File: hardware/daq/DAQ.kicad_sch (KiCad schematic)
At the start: 185 parts, among them J1 ICD15S13E4GX00LF, J2 ICD15S13E4GX00LF, J4 ICD15S13E4GX00LF, J5 ICD15S13E4GX00LF, P1 0022272021, U1 ADS124S08IRHBT, U11 SN74AHCT125RGYR, U2 ADS124S08IRHBT, U3 LT6654BMPS6-5-TRMPBF, U4 LM1086IS-5.0_NOPB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

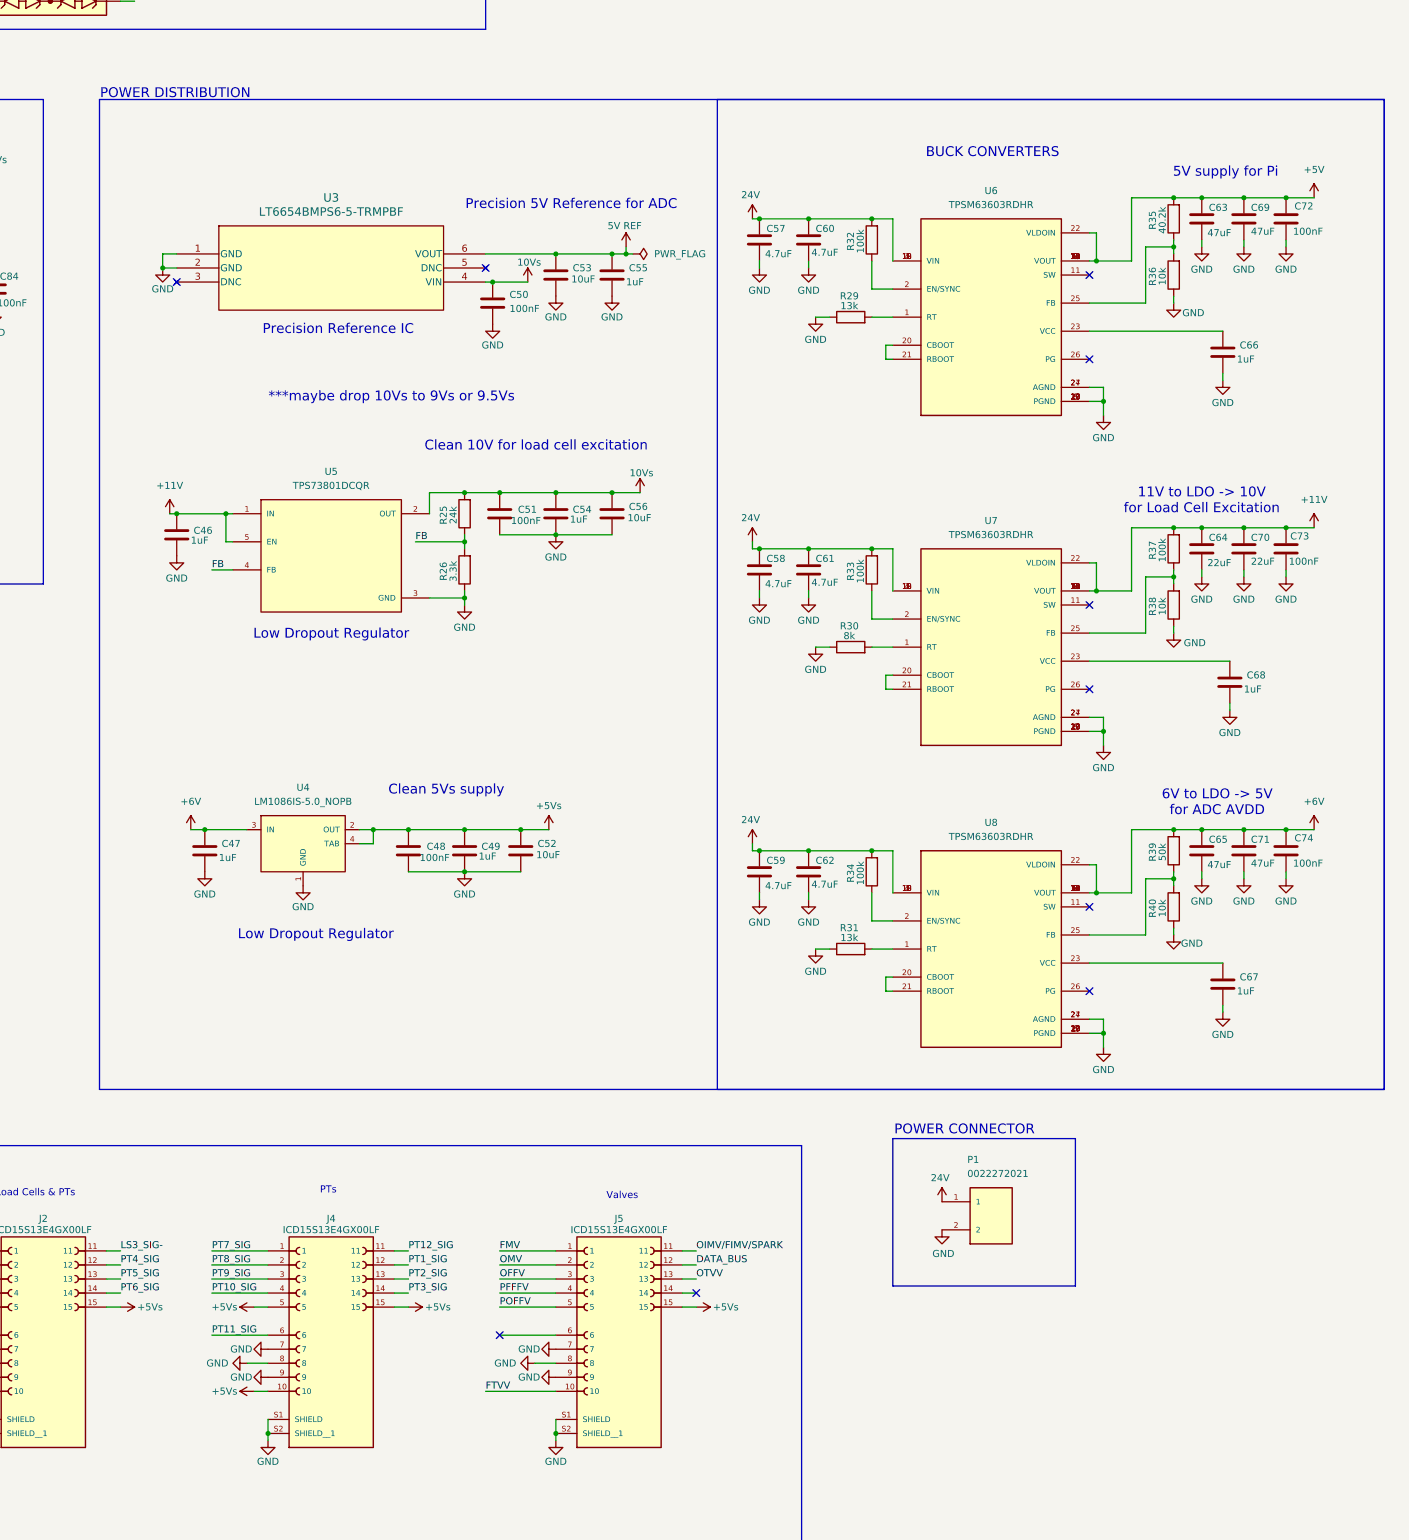
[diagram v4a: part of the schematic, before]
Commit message: more ERC fixes
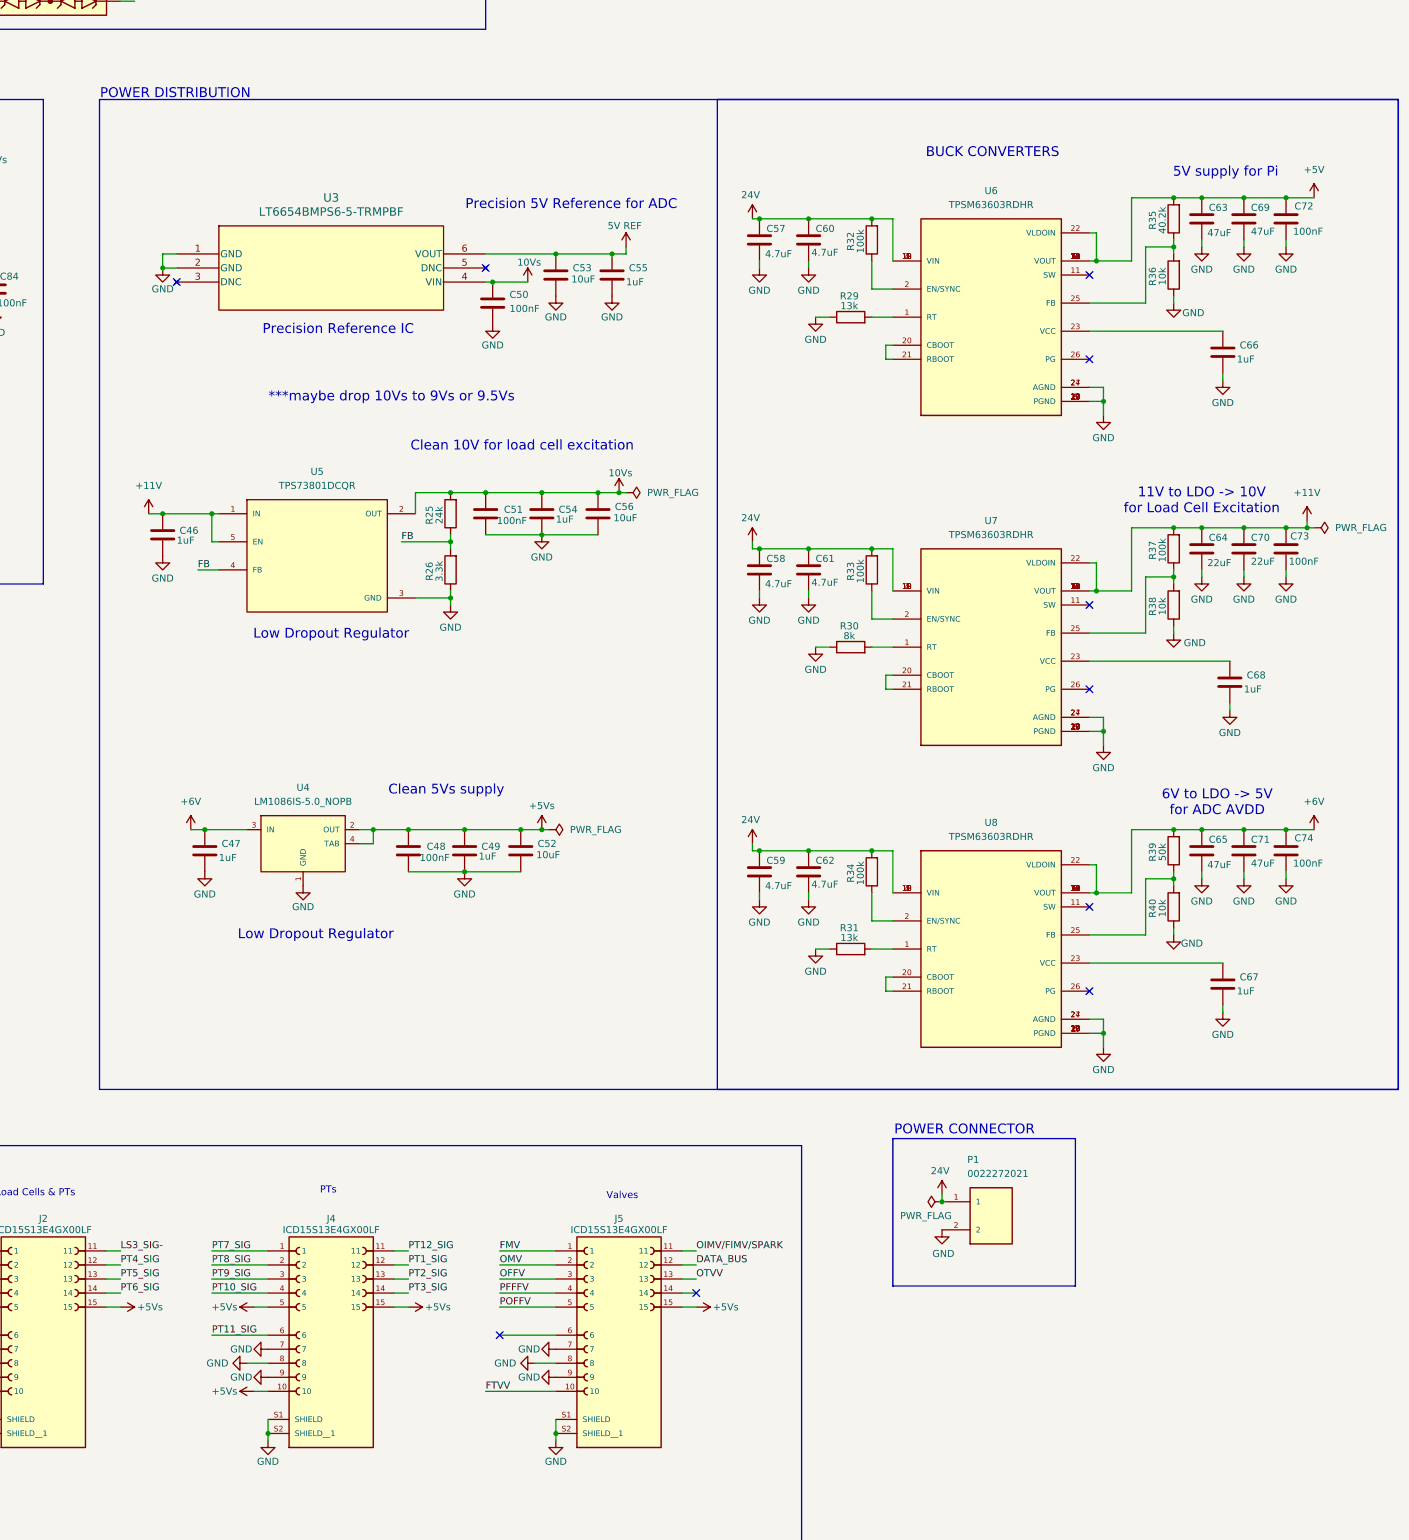
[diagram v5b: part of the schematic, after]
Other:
- moved on the sheet: C46, C51, C54, C56, R25, R26, U5

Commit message: updated layout with new ESD components w/ no errors
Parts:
- C10, C11, C12, C13, C7, C8, C85, C86, C9: footprint footprintsCL10:CAP_CL10_SAM -> Capacitor_SMD:C_0603_1608Metric_Pad1.08x0.95mm_HandSolder
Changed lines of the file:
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@@
 			)
 		)
-		(property "Footprint" "footprintsCL10:CAP_CL10_SAM"
+		(property "Footprint" "Capacitor_SMD:C_0603_1608Metric_Pad1.08x0.95mm_HandSolder"
 			(at 67.0052 95.25 0)
 			(effects
@@
 			)
 		)
-		(property "Footprint" "footprintsCL10:CAP_CL10_SAM"
+		(property "Footprint" "Capacitor_SMD:C_0603_1608Metric_Pad1.08x0.95mm_HandSolder"
 			(at 70.8152 149.86 0)
 			(effects
@@
 			)
 		)
-		(property "Footprint" "footprintsCL10:CAP_CL10_SAM"
+		(property "Footprint" "Capacitor_SMD:C_0603_1608Metric_Pad1.08x0.95mm_HandSolder"
 			(at 73.3552 297.18 0)
 			(effects
@@
 			)
 		)
-		(property "Footprint" "footprintsCL10:CAP_CL10_SAM"
+		(property "Footprint" "Capacitor_SMD:C_0603_1608Metric_Pad1.08x0.95mm_HandSolder"
 			(at 73.3552 278.13 0)
 			(effects
@@
 			)
 		)
-		(property "Footprint" "footprintsCL10:CAP_CL10_SAM"
+		(property "Footprint" "Capacitor_SMD:C_0603_1608Metric_Pad1.08x0.95mm_HandSolder"
 			(at 72.0852 58.42 0)
 			(effects
@@
 			)
 		)
-		(property "Footprint" "footprintsCL10:CAP_CL10_SAM"
+		(property "Footprint" "Capacitor_SMD:C_0603_1608Metric_Pad1.08x0.95mm_HandSolder"
 			(at 70.8152 168.91 0)
 			(effects
@@
 			)
 		)
-		(property "Footprint" "footprintsCL10:CAP_CL10_SAM"
+		(property "Footprint" "Capacitor_SMD:C_0603_1608Metric_Pad1.08x0.95mm_HandSolder"
 			(at 67.0052 111.76 0)
 			(effects
@@
 			)
 		)
-		(property "Footprint" "footprintsCL10:CAP_CL10_SAM"
+		(property "Footprint" "Capacitor_SMD:C_0603_1608Metric_Pad1.08x0.95mm_HandSolder"
 			(at 72.0852 76.2 0)
 			(effects
@@
 			)
 		)
-		(property "Footprint" "footprintsCL10:CAP_CL10_SAM"
+		(property "Footprint" "Capacitor_SMD:C_0603_1608Metric_Pad1.08x0.95mm_HandSolder"
 			(at 67.0052 128.27 0)
 			(effects

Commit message: ROUTED ADC3 BAYBEEE
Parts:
- added R43: 20K, CRCW060320K0FKEA:RESC1508X50N, symbol Device:R
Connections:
- net +3.3V: now also R43.2
- net CE3: now also R43.1
- net at C98.1, R61.1, U9.5 (AIN2): no longer C86.2
- net at C97.1, R60.1, U9.3 (AIN4): no longer C86.1
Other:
- moved on the sheet: C86
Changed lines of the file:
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@@
 	)
 	(junction
-		(at 72.39 289.56)
-		(diameter 0)
-		(color 0 0 0 0)
-	)
-	(junction
 		(at 135.89 283.21)
 		(diameter 0)
@@
 	)
 	(junction
-		(at 72.39 297.18)
-		(diameter 0)
-		(color 0 0 0 0)
-	)
-	(junction
 		(at 222.25 351.79)
 		(diameter 0)
@@
 	(wire
 		(pts
-			(xy 63.5 337.82) (xy 67.31 337.82)
+			(xy 553.72 82.55) (xy 556.26 82.55)
 		)
 		(stroke
@@
 	(wire
 		(pts
-			(xy 71.12 76.2) (xy 87.63 76.2)
+			(xy 63.5 337.82) (xy 67.31 337.82)
 		)
 		(stroke
@@
 	(wire
 		(pts
-			(xy 483.87 234.95) (xy 487.68 234.95)
+			(xy 71.12 76.2) (xy 87.63 76.2)
 		)
 		(stroke
@@
 	(wire
 		(pts
-			(xy 72.39 297.18) (xy 90.17 297.18)
+			(xy 483.87 234.95) (xy 487.68 234.95)
 		)
 		(stroke
@@
 	(wire
 		(pts
-			(xy 530.86 87.63) (xy 541.02 87.63)
+			(xy 537.21 90.17) (xy 542.29 90.17)
 		)
 		(stroke
@@
 	(wire
 		(pts
-			(xy 69.85 297.18) (xy 72.39 297.18)
+			(xy 69.85 297.18) (xy 90.17 297.18)
 		)
 		(stroke
@@
 	(wire
 		(pts
+			(xy 537.21 90.17) (xy 537.21 87.63)
+		)
+		(stroke
+			(width 0)
+			(type default)
+		)
+	)
+	(wire
+		(pts
 			(xy 218.44 86.36) (xy 210.82 86.36)
 		)
@@
 	(wire
 		(pts
+			(xy 539.75 87.63) (xy 539.75 85.09)
+		)
+		(stroke
+			(width 0)
+			(type default)
+		)
+	)
+	(wire
+		(pts
 			(xy 449.58 344.17) (xy 452.12 344.17)
 		)
@@
 	(wire
 		(pts
+			(xy 537.21 87.63) (xy 530.86 87.63)
+		)
+		(stroke
+			(width 0)
+			(type default)
+		)
+	)
+	(wire
+		(pts
 			(xy 426.72 378.46) (xy 426.72 377.19)
 		)
@@
 	(wire
 		(pts
-			(xy 530.86 82.55) (xy 541.02 82.55)
+			(xy 530.86 82.55) (xy 546.1 82.55)
 		)
 		(stroke
@@
 	(wire
 		(pts
-			(xy 530.86 85.09) (xy 541.02 85.09)
+			(xy 539.75 87.63) (xy 542.29 87.63)
 		)
 		(stroke
@@
 	(wire
 		(pts
+			(xy 539.75 85.09) (xy 530.86 85.09)
+		)
+		(stroke
+			(width 0)
+			(type default)
+		)
+	)
+	(wire
+		(pts
 			(xy 487.68 217.17) (xy 487.68 224.79)
 		)
@@
 	)
 	(label "START_SYNC3"
-		(at 541.02 87.63 0)
+		(at 542.29 90.17 0)
 		(effects
 			(font
@@
 	)
 	(label "START_SYNC2"
-		(at 541.02 85.09 0)
+		(at 542.29 87.63 0)
 		(effects
 			(font
@@
 	)
 	(symbol
+		(lib_id "power:+3.3V")
+		(at 556.26 82.55 0)
+		(unit 1)
+		(exclude_from_sim no)
+		(in_bom yes)
+		(on_board yes)
+		(dnp no)
+		(property "Reference" "#PWR066"
+			(at 556.26 86.36 0)
+			(effects
+				(font
+					(size 1.27 1.27)
+				)
+				(hide yes)
+			)
+		)
+		(property "Value" "+3.3V"
+			(at 556.006 78.74 0)
+			(effects
+				(font
+					(size 1.27 1.27)
+				)
+			)
+		)
+		(property "Footprint" ""
+			(at 556.26 82.55 0)
+			(effects
+				(font
+					(size 1.27 1.27)
+				)
+				(hide yes)
+			)
+		)
+		(property "Datasheet" ""
+			(at 556.26 82.55 0)
+			(effects
+				(font
+					(size 1.27 1.27)
+				)
+				(hide yes)
+			)
+		)
+		(property "Description" "Power symbol creates a global label with name \"+3.3V\""
+			(at 556.26 82.55 0)
+			(effects
+				(font
+					(size 1.27 1.27)
+				)
+				(hide yes)
+			)
+		)
+		(pin "1"
+		)
+		(instances
+			(project "DAQ"
+				(path "/98ce85a8-ddff-4ecb-9668-dd271ba07a43"
+					(reference "#PWR066")
+					(unit 1)
+				)
+			)
+		)
+	)
+	(symbol
 		(lib_name "ADS124S08IRHBT_1")
 		(lib_id "2025-01-27_01-32-37:ADS124S08IRHBT")
@@
 	(symbol
 		(lib_id "Device:C")
-		(at 72.39 293.37 0)
+		(at 72.39 293.37 90)
 		(unit 1)
 		(exclude_from_sim no)
@@
 		(dnp no)
 		(property "Reference" "C86"
-			(at 75.184 292.1 0)
+			(at 71.12 290.576 0)
 			(effects
 				(font
@@
 		)
 		(property "Value" "3.3nF"
-			(at 74.93 294.132 0)
+			(at 73.152 290.83 0)
 			(effects
 				(font
@@
 		)
 		(property "Footprint" "Capacitor_SMD:C_0603_1608Metric_Pad1.08x0.95mm_HandSolder"
-			(at 73.3552 297.18 0)
+			(at 76.2 292.4048 0)
 			(effects
 				(font
@@
 					(unit 1)
 				)
+			)
+		)
+	)
+	(symbol
+		(lib_id "Device:R")
+		(at 549.91 82.55 90)
+		(unit 1)
+		(exclude_from_sim no)
+		(in_bom yes)
+		(on_board yes)
+		(dnp no)
+		(property "Reference" "R43"
+			(at 549.656 80.518 90)
+			(effects
+				(font
+					(size 1.27 1.27)
+				)
+			)
+		)
+		(property "Value" "20K"
+			(at 549.656 84.582 90)
+			(effects
+				(font
+					(size 1.27 1.27)
+				)
+			)
+		)
+		(property "Footprint" "CRCW060320K0FKEA:RESC1508X50N"
+			(at 549.91 84.328 90)
+			(effects
+				(font
+					(size 1.27 1.27)
+				)
+				(hide yes)
+			)
+		)
+		(property "Datasheet" "~"
+			(at 549.91 82.55 0)
+			(effects
+				(font
+					(size 1.27 1.27)
+				)
+				(hide yes)
+			)
+		)
+		(property "Description" "Resistor"
+			(at 549.91 82.55 0)
+			(effects
+				(font
+					(size 1.27 1.27)
+				)
+				(hide yes)
+			)
+		)
+		(pin "1"
+		)
+		(pin "2"
+		)
+		(instances
+			(project "DAQ"
+				(path "/98ce85a8-ddff-4ecb-9668-dd271ba07a43"
+					(reference "R43")
+					(unit 1)
+				)

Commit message: routed UART conversion components
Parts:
- R52: value 1K -> 10K
- R53: value 2.2K -> 20K
- renumbered D7 to D11, D11 to D7, J4 to J3, J5 to J4
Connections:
- net +3.3V: now also R54.2; no longer R54.1
- net DRDY_N3: now also RP1.11 (GPIO_17/SPI1_CS1); no longer RP1.12 (GPIO_18/PWM0/SPI1_CS0)
- net START_SYNC1: now also RP1.33 (GPIO13/PWM1); no longer RP1.11 (GPIO_17/SPI1_CS1)
- net TX_ENABLE: now also R54.1, RP1.12 (GPIO_18/PWM0/SPI1_CS0); no longer R54.2, RP1.33 (GPIO13/PWM1)
- net at C98.1, R61.1, U9.5 (AIN2): now also C86.2
- net at C97.1, R60.1, U9.3 (AIN4): now also C86.1
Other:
- note added: "FLOW METER SHIT"
- note added: "Voltage divider to step the 5V signal from the servo serial bus to a tolerable GPIO voltage (~3.33V)"
- note removed: "Voltage divider to step the 5V signal from the servo serial bus to a tolerable GPIO voltage (~3.44V)"
- moved on the sheet: C84, C86, D10, D5, D6, D9, H1, H2, H3, H4, P1, R52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
